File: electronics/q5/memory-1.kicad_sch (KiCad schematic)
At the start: 5 parts, among them U8 SPI F-RAM 32KiB

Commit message: Q5 design lock: JLC Basic substitutions, re-verified board, cost estimator
Co-Authored-By: Claude Opus 5.5 <noreply@anthropic.com>
Claude-Session: https://claude.ai/code/session_01UrkzLMrBi6iLPSL5SbMCA7
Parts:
- C36: MPN GRM188R71H104KA93D -> CC0603KRX7R9BB104
- R33: MPN RC0603FR-07100KL -> 0603WAF1003T5E
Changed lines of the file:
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@@
       (in_bom yes) (on_board yes) (dnp no)
  (property "Reference" "C36" (at 294.64 73.66 0) (effects (font (size 1.524 1.524)))) (property "Value" "100n" (at 294.64 77.46999999999998 0) (effects (font (size 1.524 1.524))))
-      (property "Footprint" "CountFidgetQ5:Capacitor_SMD_C_0603_1608Metric" (at 294.64 82.55 0) (effects (font (size 1.27 1.27)) (hide yes))) (property "MPN" "GRM188R71H104KA93D" (at 294.64 77.46999999999998 0) (effects (font (size 1.524 1.524)) (hide yes)))
+      (property "Footprint" "CountFidgetQ5:Capacitor_SMD_C_0603_1608Metric" (at 294.64 82.55 0) (effects (font (size 1.27 1.27)) (hide yes))) (property "MPN" "CC0603KRX7R9BB104" (at 294.64 77.46999999999998 0) (effects (font (size 1.524 1.524)) (hide yes)))
       (property "Description" "100nF local FRAM bypass, in addition to C30" (at 294.64 82.55 0) (effects (font (size 1.27 1.27)) (hide yes)))
       (pin "1")(pin "2")
@@
       (in_bom yes) (on_board yes) (dnp no)
  (property "Reference" "R33" (at 294.64 152.4 0) (effects (font (size 1.524 1.524)))) (property "Value" "100k" (at 294.64 156.21 0) (effects (font (size 1.524 1.524))))
-      (property "Footprint" "CountFidgetQ5:Resistor_SMD_R_0603_1608Metric" (at 294.64 161.29 0) (effects (font (size 1.27 1.27)) (hide yes))) (property "MPN" "RC0603FR-07100KL" (at 294.64 156.21 0) (effects (font (size 1.524 1.524)) (hide yes)))
+      (property "Footprint" "CountFidgetQ5:Resistor_SMD_R_0603_1608Metric" (at 294.64 161.29 0) (effects (font (size 1.27 1.27)) (hide yes))) (property "MPN" "0603WAF1003T5E" (at 294.64 156.21 0) (effects (font (size 1.524 1.524)) (hide yes)))
       (property "Description" "100k external pull-up; MCU CS must be open-drain" (at 294.64 161.29 0) (effects (font (size 1.27 1.27)) (hide yes)))
       (pin "1")(pin "2")

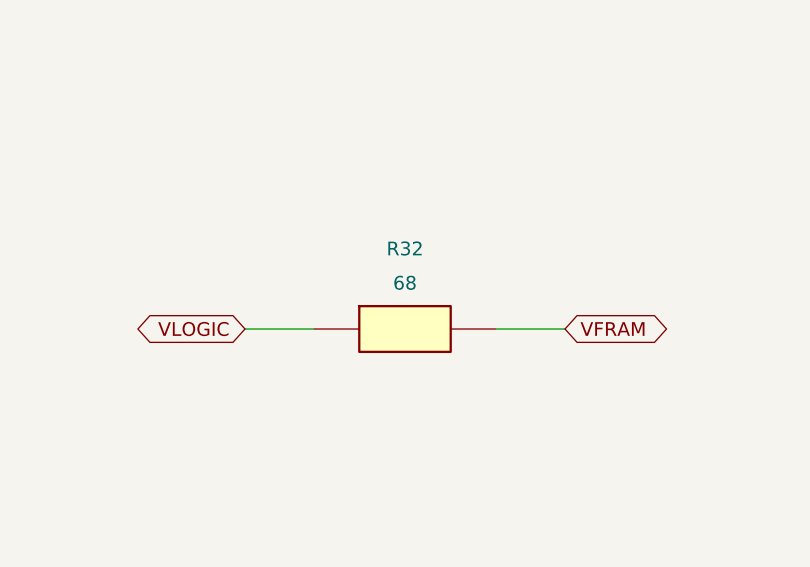
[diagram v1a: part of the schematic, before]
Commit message: Move nine part types to JLC Basic; 16 Extended types remain, each justified
R4 18k (16.7 mA charge), temperature window 56k/82k/18k/12k (7.26-35.83 C),
R32 75 ohm, Q1/Q2 AO3400A, 2.2 uF and 10 uF 50 V 0805 capacitors. Fresh
ERC/DRC/parity on unchanged routing, stock 42/42, exports, JLC footprint
fit and pin names, power/latch checks re-run. About $28 less per order.

Co-Authored-By: Claude Opus 5.5 <noreply@anthropic.com>
Claude-Session: https://claude.ai/code/session_01UrkzLMrBi6iLPSL5SbMCA7
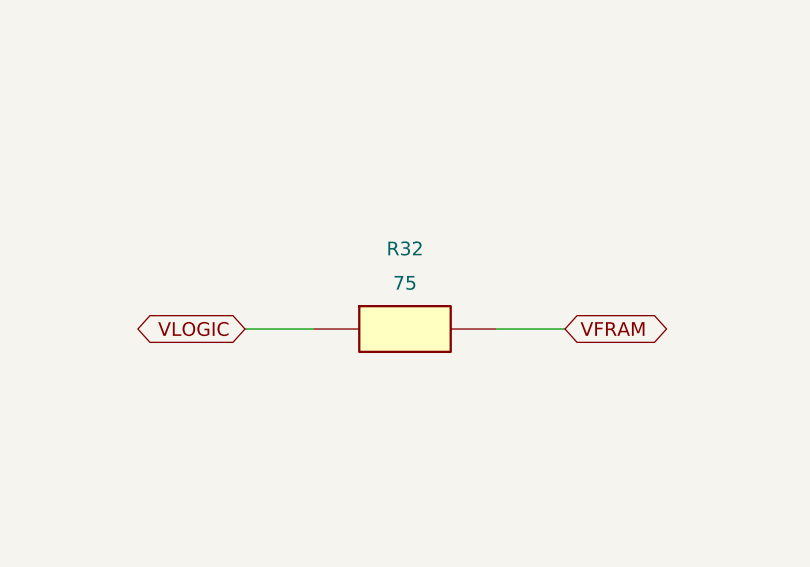
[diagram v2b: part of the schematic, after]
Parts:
- C30: MPN GRM21BR61E106KA73L -> GRM21BR61H106KE43L
- R32: value 68 -> 75; MPN 0603WAF680JT5E -> 0603WAF750JT5E
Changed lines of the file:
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@@
       (in_bom yes) (on_board yes) (dnp no)
  (property "Reference" "C30" (at 105.41 73.66 0) (effects (font (size 1.524 1.524)))) (property "Value" "10u" (at 105.41 77.46999999999998 0) (effects (font (size 1.524 1.524))))
-      (property "Footprint" "CountFidgetQ5:Capacitor_SMD_C_0805_2012Metric" (at 105.41 82.55 0) (effects (font (size 1.27 1.27)) (hide yes))) (property "MPN" "GRM21BR61E106KA73L" (at 105.41 77.46999999999998 0) (effects (font (size 1.524 1.524)) (hide yes)))
-      (property "Description" "10uF25V X5R; require>=6.8uF effective for proposed memory ramp budget" (at 105.41 82.55 0) (effects (font (size 1.27 1.27)) (hide yes)))
+      (property "Footprint" "CountFidgetQ5:Capacitor_SMD_C_0805_2012Metric" (at 105.41 82.55 0) (effects (font (size 1.27 1.27)) (hide yes))) (property "MPN" "GRM21BR61H106KE43L" (at 105.41 77.46999999999998 0) (effects (font (size 1.524 1.524)) (hide yes)))
+      (property "Description" "10 uF 50 V X5R; require >=6.8 uF effective at the memory rail (measure on the first article)" (at 105.41 82.55 0) (effects (font (size 1.27 1.27)) (hide yes)))
       (pin "1")(pin "2")
       (instances (project "click-counter-Q5" (path "/7c190cd8-3ca2-5363-8a92-396d30a08243/dfe44b2e-dca8-55dc-a058-ba49538b1523" (reference "C30") (unit 1)))))
@@
 (symbol (lib_id "CountFidgetQ5:R32") (at 105.41 161.29 0) (unit 1) (exclude_from_sim no)
       (in_bom yes) (on_board yes) (dnp no)
- (property "Reference" "R32" (at 105.41 152.4 0) (effects (font (size 1.524 1.524)))) (property "Value" "68" (at 105.41 156.21 0) (effects (font (size 1.524 1.524))))
-      (property "Footprint" "CountFidgetQ5:Resistor_SMD_R_0603_1608Metric" (at 105.41 161.29 0) (effects (font (size 1.27 1.27)) (hide yes))) (property "MPN" "0603WAF680JT5E" (at 105.41 156.21 0) (effects (font (size 1.524 1.524)) (hide yes)))
-      (property "Description" "1%; controlled memory rail RC" (at 105.41 161.29 0) (effects (font (size 1.27 1.27)) (hide yes)))
+ (property "Reference" "R32" (at 105.41 152.4 0) (effects (font (size 1.524 1.524)))) (property "Value" "75" (at 105.41 156.21 0) (effects (font (size 1.524 1.524))))
+      (property "Footprint" "CountFidgetQ5:Resistor_SMD_R_0603_1608Metric" (at 105.41 161.29 0) (effects (font (size 1.27 1.27)) (hide yes))) (property "MPN" "0603WAF750JT5E" (at 105.41 156.21 0) (effects (font (size 1.524 1.524)) (hide yes)))
+      (property "Description" "1%; controlled memory rail RC (75 ohm with C30)" (at 105.41 161.29 0) (effects (font (size 1.27 1.27)) (hide yes)))
       (pin "1")(pin "2")
       (instances (project "click-counter-Q5" (path "/7c190cd8-3ca2-5363-8a92-396d30a08243/dfe44b2e-dca8-55dc-a058-ba49538b1523" (reference "R32") (unit 1)))))
